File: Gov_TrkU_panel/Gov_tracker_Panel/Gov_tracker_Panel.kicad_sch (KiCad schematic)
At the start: 4 parts

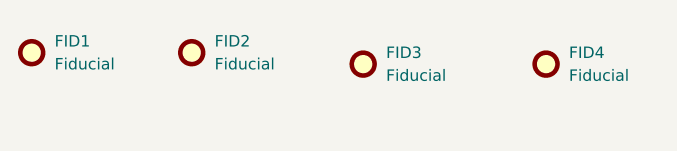
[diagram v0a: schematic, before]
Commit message: updated the pannel and generated gerber files
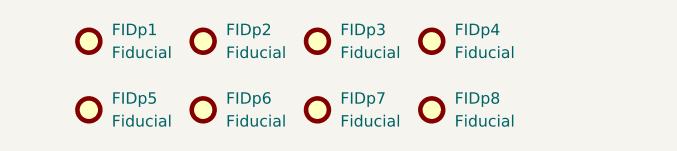
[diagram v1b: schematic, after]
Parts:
- removed FID1: Fiducial, Fiducial:Fiducial_0.75mm_Mask1.5mm, symbol Mechanical:Fiducial
- added FIDp1, FIDp5, FIDp6, FIDp7, FIDp8: Fiducial, Fiducial:Fiducial_0.75mm_Mask1.5mm, symbol Mechanical:Fiducial
- renumbered FID2 to FIDp2, FID3 to FIDp3, FID4 to FIDp4
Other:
- moved on the sheet: FIDp2, FIDp3, FIDp4
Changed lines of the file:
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@@
 (kicad_sch (version 20230121) (generator eeschema)
   (paper "A4")
-  (symbol (lib_id "Mechanical:Fiducial") (at 76.2 115.57 0) (unit 1)
+  (symbol (lib_id "Mechanical:Fiducial") (at 77.47 114.3 0) (unit 1)
     (in_bom yes) (on_board yes) (dnp no) (fields_autoplaced)
-    (property "Reference" "FID2" (at 78.74 114.3 0)
+    (property "Reference" "FIDp2" (at 80.01 113.03 0)
       (effects (font (size 1.27 1.27)) (justify left))
     )
-    (property "Value" "Fiducial" (at 78.74 116.84 0)
+    (property "Value" "Fiducial" (at 80.01 115.57 0)
       (effects (font (size 1.27 1.27)) (justify left))
     )
-    (property "Footprint" "Fiducial:Fiducial_0.75mm_Mask1.5mm" (at 76.2 115.57 0)
+    (property "Footprint" "Fiducial:Fiducial_0.75mm_Mask1.5mm" (at 77.47 114.3 0)
       (effects (font (size 1.27 1.27)) hide)
     )
-    (property "Datasheet" "~" (at 76.2 115.57 0)
+    (property "Datasheet" "~" (at 77.47 114.3 0)
       (effects (font (size 1.27 1.27)) hide)
     )
@@
       (project "Gov_tracker_Panel"
         (path "/1200383d-80a4-407c-a537-8b2d3c67094d"
-          (reference "FID2") (unit 1)
+          (reference "FIDp2") (unit 1)
         )
       )
     )
   )
-  (symbol (lib_id "Mechanical:Fiducial") (at 58.42 115.57 0) (unit 1)
+  (symbol (lib_id "Mechanical:Fiducial") (at 64.77 114.3 0) (unit 1)
     (in_bom yes) (on_board yes) (dnp no) (fields_autoplaced)
-    (property "Reference" "FID1" (at 60.96 114.3 0)
+    (property "Reference" "FIDp1" (at 67.31 113.03 0)
       (effects (font (size 1.27 1.27)) (justify left))
     )
-    (property "Value" "Fiducial" (at 60.96 116.84 0)
+    (property "Value" "Fiducial" (at 67.31 115.57 0)
       (effects (font (size 1.27 1.27)) (justify left))
     )
-    (property "Footprint" "Fiducial:Fiducial_0.75mm_Mask1.5mm" (at 58.42 115.57 0)
+    (property "Footprint" "Fiducial:Fiducial_0.75mm_Mask1.5mm" (at 64.77 114.3 0)
       (effects (font (size 1.27 1.27)) hide)
     )
-    (property "Datasheet" "~" (at 58.42 115.57 0)
+    (property "Datasheet" "~" (at 64.77 114.3 0)
       (effects (font (size 1.27 1.27)) hide)
     )
@@
       (project "Gov_tracker_Panel"
         (path "/1200383d-80a4-407c-a537-8b2d3c67094d"
-          (reference "FID1") (unit 1)
+          (reference "FIDp1") (unit 1)
         )
       )
     )
   )
-  (symbol (lib_id "Mechanical:Fiducial") (at 95.25 116.84 0) (unit 1)
+  (symbol (lib_id "Mechanical:Fiducial") (at 90.17 114.3 0) (unit 1)
     (in_bom yes) (on_board yes) (dnp no) (fields_autoplaced)
-    (property "Reference" "FID3" (at 97.79 115.57 0)
+    (property "Reference" "FIDp3" (at 92.71 113.03 0)
       (effects (font (size 1.27 1.27)) (justify left))
     )
-    (property "Value" "Fiducial" (at 97.79 118.11 0)
+    (property "Value" "Fiducial" (at 92.71 115.57 0)
       (effects (font (size 1.27 1.27)) (justify left))
     )
-    (property "Footprint" "Fiducial:Fiducial_0.75mm_Mask1.5mm" (at 95.25 116.84 0)
+    (property "Footprint" "Fiducial:Fiducial_0.75mm_Mask1.5mm" (at 90.17 114.3 0)
       (effects (font (size 1.27 1.27)) hide)
     )
-    (property "Datasheet" "~" (at 95.25 116.84 0)
+    (property "Datasheet" "~" (at 90.17 114.3 0)
       (effects (font (size 1.27 1.27)) hide)
     )
@@
       (project "Gov_tracker_Panel"
         (path "/1200383d-80a4-407c-a537-8b2d3c67094d"
-          (reference "FID3") (unit 1)
+          (reference "FIDp3") (unit 1)
         )
       )
     )
   )
-  (symbol (lib_id "Mechanical:Fiducial") (at 115.57 116.84 0) (unit 1)
+  (symbol (lib_id "Mechanical:Fiducial") (at 102.87 121.92 0) (unit 1)
     (in_bom yes) (on_board yes) (dnp no) (fields_autoplaced)
-    (property "Reference" "FID4" (at 118.11 115.57 0)
+    (property "Reference" "FIDp8" (at 105.41 120.65 0)
       (effects (font (size 1.27 1.27)) (justify left))
     )
-    (property "Value" "Fiducial" (at 118.11 118.11 0)
+    (property "Value" "Fiducial" (at 105.41 123.19 0)
       (effects (font (size 1.27 1.27)) (justify left))
     )
-    (property "Footprint" "Fiducial:Fiducial_0.75mm_Mask1.5mm" (at 115.57 116.84 0)
+    (property "Footprint" "Fiducial:Fiducial_0.75mm_Mask1.5mm" (at 102.87 121.92 0)
       (effects (font (size 1.27 1.27)) hide)
     )
-    (property "Datasheet" "~" (at 115.57 116.84 0)
+    (property "Datasheet" "~" (at 102.87 121.92 0)
       (effects (font (size 1.27 1.27)) hide)
     )
@@
       (project "Gov_tracker_Panel"
         (path "/1200383d-80a4-407c-a537-8b2d3c67094d"
-          (reference "FID4") (unit 1)
+          (reference "FIDp8") (unit 1)
         )
       )
+    )
+  )
+  (symbol (lib_id "Mechanical:Fiducial") (at 64.77 121.92 0) (unit 1)
+    (in_bom yes) (on_board yes) (dnp no) (fields_autoplaced)
+    (property "Reference" "FIDp5" (at 67.31 120.65 0)
+      (effects (font (size 1.27 1.27)) (justify left))
+    )
+    (property "Value" "Fiducial" (at 67.31 123.19 0)
+      (effects (font (size 1.27 1.27)) (justify left))
+    )
+    (property "Footprint" "Fiducial:Fiducial_0.75mm_Mask1.5mm" (at 64.77 121.92 0)
+      (effects (font (size 1.27 1.27)) hide)
+    )
+    (property "Datasheet" "~" (at 64.77 121.92 0)
+      (effects (font (size 1.27 1.27)) hide)
+    )
+    (instances
+      (project "Gov_tracker_Panel"
+        (path "/1200383d-80a4-407c-a537-8b2d3c67094d"
+          (reference "FIDp5") (unit 1)
+        )
+      )
+    )
+  )
+  (symbol (lib_id "Mechanical:Fiducial") (at 90.17 121.92 0) (unit 1)
+    (in_bom yes) (on_board yes) (dnp no) (fields_autoplaced)
+    (property "Reference" "FIDp7" (at 92.71 120.65 0)
+      (effects (font (size 1.27 1.27)) (justify left))
+    )
+    (property "Value" "Fiducial" (at 92.71 123.19 0)
+      (effects (font (size 1.27 1.27)) (justify left))
+    )
+    (property "Footprint" "Fiducial:Fiducial_0.75mm_Mask1.5mm" (at 90.17 121.92 0)
+      (effects (font (size 1.27 1.27)) hide)
+    )
+    (property "Datasheet" "~" (at 90.17 121.92 0)
+      (effects (font (size 1.27 1.27)) hide)
+    )
+    (instances
+      (project "Gov_tracker_Panel"
+        (path "/1200383d-80a4-407c-a537-8b2d3c67094d"
+          (reference "FIDp7") (unit 1)
+        )
+      )
+    )
+  )
+  (symbol (lib_id "Mechanical:Fiducial") (at 77.47 121.92 0) (unit 1)
+    (in_bom yes) (on_board yes) (dnp no) (fields_autoplaced)
+    (property "Reference" "FIDp6" (at 80.01 120.65 0)
+      (effects (font (size 1.27 1.27)) (justify left))
+    )
+    (property "Value" "Fiducial" (at 80.01 123.19 0)
+      (effects (font (size 1.27 1.27)) (justify left))
+    )
+    (property "Footprint" "Fiducial:Fiducial_0.75mm_Mask1.5mm" (at 77.47 121.92 0)
+      (effects (font (size 1.27 1.27)) hide)
+    )
+    (property "Datasheet" "~" (at 77.47 121.92 0)
+      (effects (font (size 1.27 1.27)) hide)
+    )
+    (instances
+      (project "Gov_tracker_Panel"
+        (path "/1200383d-80a4-407c-a537-8b2d3c67094d"
+          (reference "FIDp6") (unit 1)
+        )
+      )
+    )
+  )
+  (symbol (lib_id "Mechanical:Fiducial") (at 102.87 114.3 0) (unit 1)
+    (in_bom yes) (on_board yes) (dnp no) (fields_autoplaced)
+    (property "Reference" "FIDp4" (at 105.41 113.03 0)
+      (effects (font (size 1.27 1.27)) (justify left))
+    )
+    (property "Value" "Fiducial" (at 105.41 115.57 0)
+      (effects (font (size 1.27 1.27)) (justify left))
+    )
+    (property "Footprint" "Fiducial:Fiducial_0.75mm_Mask1.5mm" (at 102.87 114.3 0)
+      (effects (font (size 1.27 1.27)) hide)
+    )
+    (property "Datasheet" "~" (at 102.87 114.3 0)
+      (effects (font (size 1.27 1.27)) hide)
+    )
+    (instances
+      (project "Gov_tracker_Panel"
+        (path "/1200383d-80a4-407c-a537-8b2d3c67094d"
+          (reference "FIDp4") (unit 1)
+        )
+      )
